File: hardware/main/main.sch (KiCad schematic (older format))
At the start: 62 parts, among them J1 Conn_01x10, J10 Conn_01x02, J11 Conn_01x02, J2 Conn_01x10, J3 Conn_01x02, J4 USB_B_Micro, J5 Conn_01x04, J6 Conn_01x03, J7 Conn_01x02, J8 Conn_01x03, J9 Conn_01x02, K1 G6SU-2, K2 G6SU-2, K3 G6SU-2, K4 G6SU-2, K5 G6SU-2, K6 G6SU-2, K7 G6SU-2, K8 G6SU-2, SW1 Rotary_Encoder_Switch, U1 NCV7726B, U10 SP3485EN, U2 MAX98357A, U3 MOC3043M, U4 SP3485EN, U5 E73-2G4M08S1C-52840, U6 BME680, U7 TPS82130, U8 D203S, U9 UG-2864ASWPG01

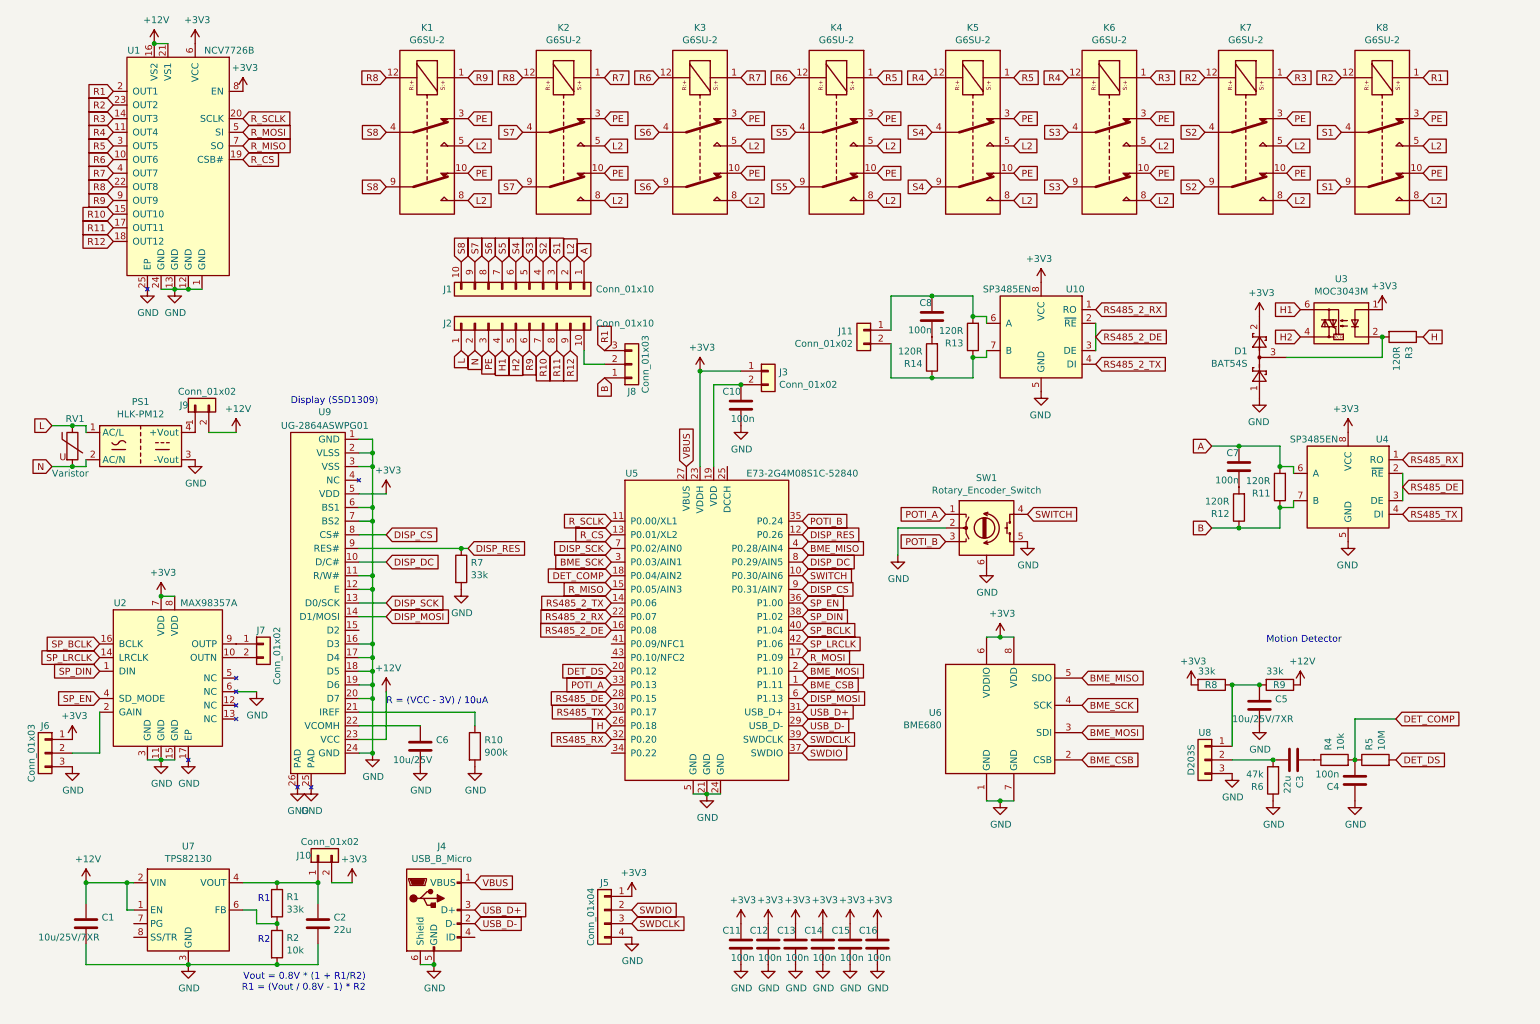
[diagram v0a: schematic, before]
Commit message: Update main board to use LIN
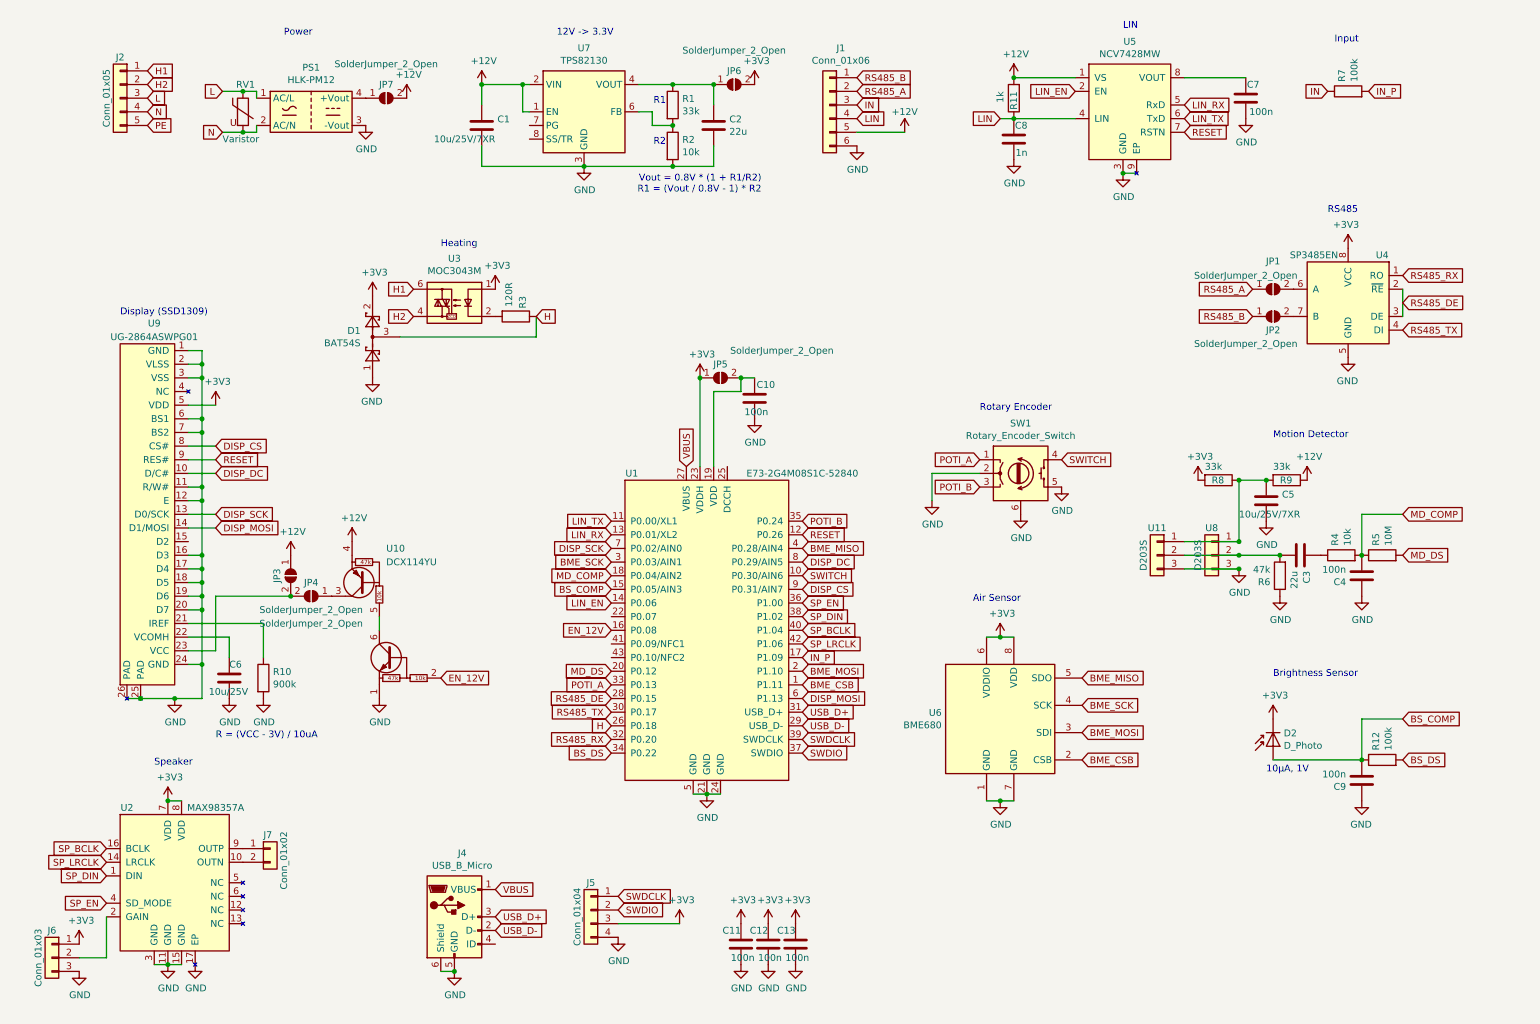
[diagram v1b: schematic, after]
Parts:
- removed C14, C15, C16: 100n, Capacitor_SMD:C_0603_1608Metric, symbol Device:C
- removed J1, J2: Conn_01x10, RoomControl:WAGO-236-410, symbol Connector_Generic:Conn_01x10
- removed J10, J3, J9: Conn_01x02, RoomControl:Jumper2, symbol Connector_Generic:Conn_01x02
- removed J11: Conn_01x02, Connector_PinHeader_2.54mm:PinHeader_1x02_P2.54mm_Vertical, symbol Connector_Generic:Conn_01x02
- removed J8: Conn_01x03, RoomControl:Jumper3, symbol Connector_Generic:Conn_01x03
- removed K1, K2, K3, K4, K5, K6, K7, K8: G6SU-2, RoomControl:Relay_DPDT_Omron_G6SU-2, symbol Relay:G6SU-2
- removed R13: 120R, Resistor_SMD:R_1206_3216Metric, symbol Device:R
- removed R14: 120R, Resistor_SMD:R_0603_1608Metric, symbol Device:R
- removed U1: NCV7726B, RoomControl:NCV7726B, symbol RoomControl:NCV7726B
- removed U10: SP3485EN, Package_SO:SOIC-8_3.9x4.9mm_P1.27mm, symbol Interface_UART:SP3485EN
- added C9: 100n, Capacitor_SMD:C_0603_1608Metric, symbol Device:C
- added D2: D_Photo, Connector_PinHeader_2.54mm:PinHeader_1x02_P2.54mm_Vertical, symbol Device:D_Photo
- added J1: Conn_01x06, RoomControl:Wago_236-406, symbol Connector_Generic:Conn_01x06
- added J2: Conn_01x05, RoomControl:Wago_236-405, symbol Connector_Generic:Conn_01x05
- added JP1, JP2, JP3, JP4, JP5, JP6, JP7: SolderJumper_2_Open, RoomControl:Jumper2Triangular, symbol Jumper:SolderJumper_2_Open
- added U10: DCX114YU, Package_TO_SOT_SMD:SOT-363_SC-70-6, symbol RoomControl:DCX114YU
- added U11: D203S, RoomControl:D203S, symbol Connector_Generic:Conn_01x03
- added U5: NCV7428MW, Package_DFN_QFN:DFN-8-1EP_3x3mm_P0.65mm_EP1.55x2.4mm, symbol RoomControl:NCV7428MW
- C8: value 100n -> 1n
- PS1: footprint Converter_ACDC:Converter_ACDC_HiLink_HLK-PMxx -> RoomControl:Converter_ACDC_HiLink_HLK-PMxx
- R11: value 120R -> 1k; footprint Resistor_SMD:R_1206_3216Metric -> Resistor_SMD:R_0603_1608Metric
- R12: value 120R -> 100k
- R7: value 33k -> 100k; footprint Resistor_SMD:R_0603_1608Metric -> Resistor_SMD:R_1206_3216Metric
- renumbered U5 to U1
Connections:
- net +12V: now also R11.2, J1.5 (Pin_5), JP3.1 (A), JP7.2 (B), U10.4 (C2), U5.1 (VS); no longer U9.23 (VCC)
- net +3V3: now also J5.3 (Pin_3), D2.1 (K), JP5.1 (A), JP6.2 (B); no longer J5.1 (Pin_1)
- net GND: now also C7.1, C8.1, C9.1, J1.6 (Pin_6), U10.1 (E1), U11.3 (Pin_3), U5.3 (GND), U5.9 (EP); no longer R7.2, U2.6 (NC)
- net H: now also D1.3
- net H1: now also J2.1 (Pin_1)
- net H2: now also J2.2 (Pin_2)
- net L: now also J2.3 (Pin_3)
- net N: now also J2.4 (Pin_4)
- net PE: now also J2.5 (Pin_5)
- net SWDCLK: now also J5.1 (Pin_1); no longer J5.3 (Pin_3)
- net at C2.1, R1.1, U7.4 (VOUT)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: now also JP6.1 (A)
- net at PS1.4 (+Vout): now also JP7.1 (A)
- net at R3.2, U3.2: no longer D1.3
- net at C10.2, U1.19 (VDD): now also JP5.2 (B)
- net BS_DS: now reaches U1.34 (P0.22)
- net BS_DS: now also R12.2
- net at C3.2, R6.2, U8.2 (Pin_2): now also U11.2 (Pin_2)
- net at C5.1, R8.1, R9.2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: now also U11.1 (Pin_1)
- net LIN: now reaches C8.2
- net LIN: now also R11.1, J1.4 (Pin_4), U5.4 (LIN)
- removed net A: C7.2, R11.2, U4.6 (A)
- removed net B: R11.1, R12.1, U4.7 (B)
- net DET_COMP renamed MD_COMP
- net DET_DS renamed MD_DS
- net DISP_RES renamed RESET
- net RESET: now also U5.7 (RSTN); no longer R7.1
- net RS485_2_DE renamed EN_12V
- net EN_12V: now also U10.2 (B1)
- net RS485_2_RX: no longer names the net of U1.22 (P0.07)
- net RS485_2_TX renamed LIN_EN
- net LIN_EN: now also U5.2 (EN)
- net R_CS renamed LIN_RX
- net LIN_RX: now also U5.5 (RxD)
- net R_MISO renamed BS_COMP
- net BS_COMP: now also R12.1, C9.2, D2.2 (A)
- net R_MOSI renamed IN_P
- net IN_P: now also R7.2
- net R_SCLK renamed LIN_TX
- net LIN_TX: now also U5.6 (TxD)
- new net: JP1.2 (B), U4.6 (A)
- new net: JP2.2 (B), U4.7 (B)
- new net: JP3.2 (B), JP4.2 (B), U9.23 (VCC)
- new net: C7.2, U5.8 (VOUT)
- new net: JP4.1 (A), U10.3 (C2)
- new net: U10.5 (B2), U10.6 (C1)
- new net IN: J1.3 (Pin_3), R7.1
- new net RS485_A: J1.2 (Pin_2), JP1.1 (A)
- new net RS485_B: J1.1 (Pin_1), JP2.1 (A)
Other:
- note added: "10µA, 1V"
- note added: "12V -> 3.3V"
- note added: "Air Sensor"
- note added: "Brightness Sensor"
- note added: "Heating"
- note added: "Input"
- note added: "LIN"
- note added: "Power"
- note added: "RS485"
- note added: "Rotary Encoder"
- note added: "Speaker"
- moved on the sheet: C1, C10, C2, C3, C4, C5, C6, D1, J4, J5, J6, J7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

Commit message: Add backup battery and 32768Hz crystal
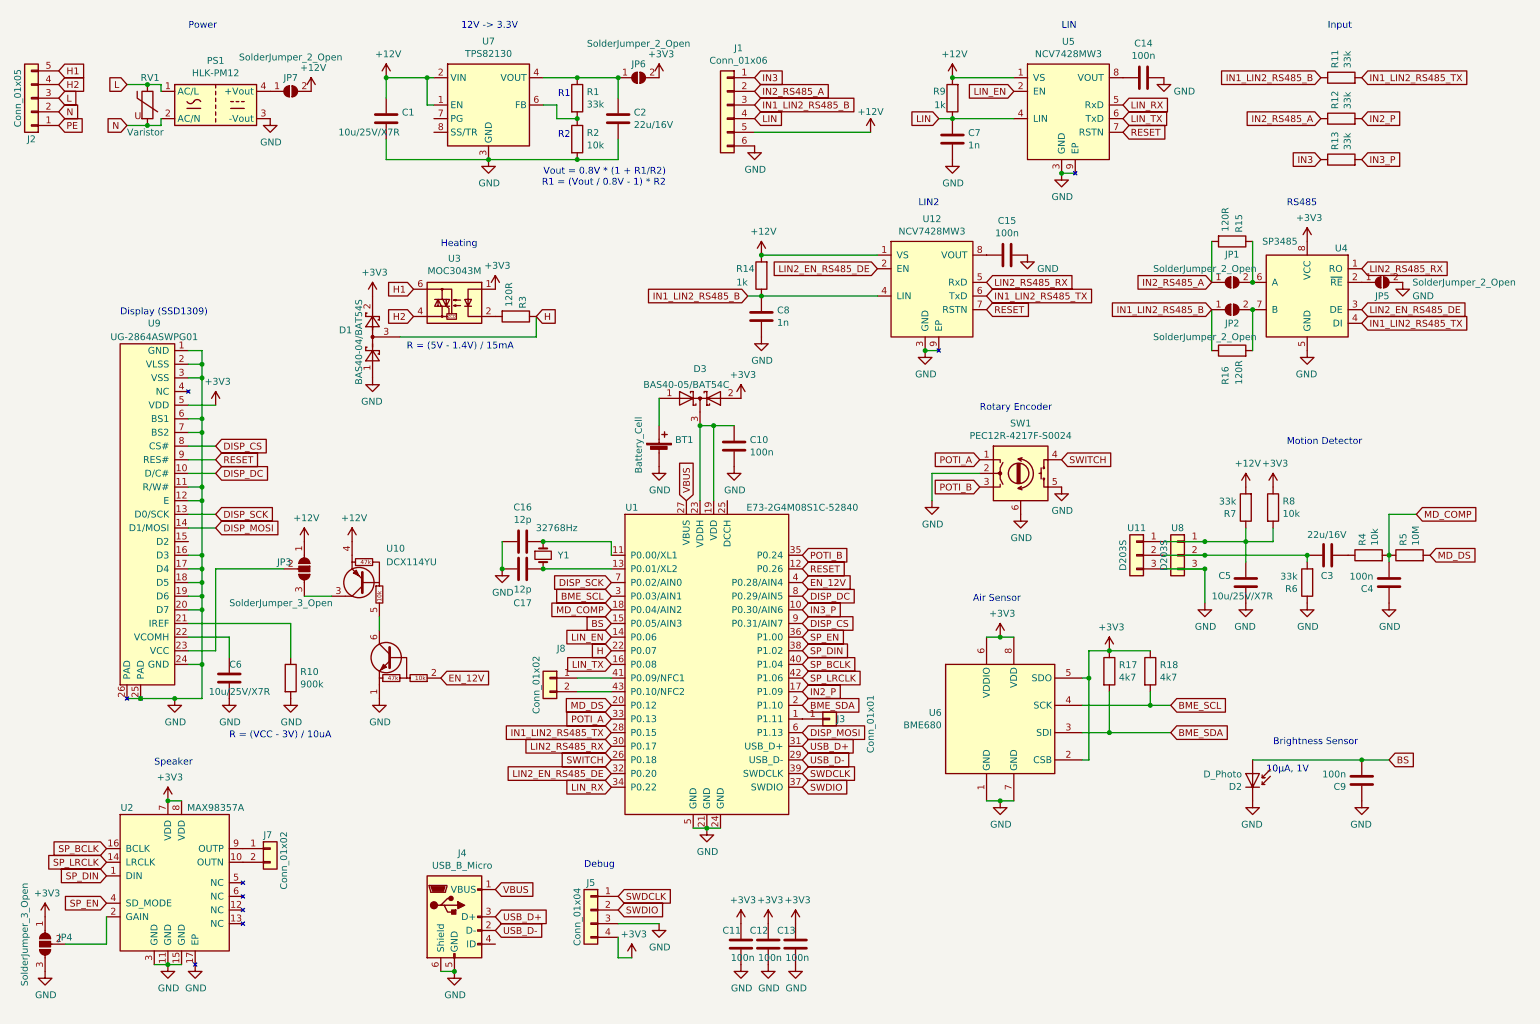
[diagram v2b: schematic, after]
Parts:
- removed J6: Conn_01x03, RoomControl:Jumper3, symbol Connector_Generic:Conn_01x03
- removed JP3, JP4: SolderJumper_2_Open, RoomControl:Jumper2Triangular, symbol Jumper:SolderJumper_2_Open
- removed R11: 1k, Resistor_SMD:R_0603_1608Metric, symbol Device:R
- added BT1: Battery_Cell, RoomControl:Battery_2032, symbol Device:Battery_Cell
- added C14, C15: 100n, Capacitor_SMD:C_0603_1608Metric, symbol Device:C
- added C16, C17: 12p, Capacitor_SMD:C_0603_1608Metric, symbol Device:C
- added D3: BAS40-05/BAT54C, Package_TO_SOT_SMD:SOT-23, symbol Device:D_Schottky_x2_KCom_AAK
- added J3: Conn_01x01, RoomControl:Pad, symbol Connector_Generic:Conn_01x01
- added J8: Conn_01x02, Connector_PinHeader_2.00mm:PinHeader_1x02_P2.00mm_Vertical, symbol Connector_Generic:Conn_01x02
- added JP3, JP4: SolderJumper_3_Open, RoomControl:Jumper3, symbol Jumper:SolderJumper_3_Open
- added R13: 33k, Resistor_SMD:R_1206_3216Metric, symbol Device:R
- added R14: 1k, Resistor_SMD:R_1206_3216Metric, symbol Device:R
- added R15, R16: 120R, Resistor_SMD:R_1206_3216Metric, symbol Device:R
- added R17, R18: 4k7, Resistor_SMD:R_0603_1608Metric, symbol Device:R
- added R7: 33k, Resistor_SMD:R_0603_1608Metric, symbol Device:R
- added U12: NCV7428MW3, RoomControl:On_NCV7428MW, symbol RoomControl:NCV7428MW
- added Y1: 32768Hz, Crystal:Crystal_DS26_D2.0mm_L6.0mm_Vertical, symbol Device:Crystal_Small
- C1, C5: value 10u/25V/7XR -> 10u/25V/X7R
- C2, C3: value 22u -> 22u/16V
- C6: value 10u/25V -> 10u/25V/X7R
- C7: value 100n -> 1n
- D1: value BAT54S -> BAS40-04/BAT54S
- JP1, JP2, JP5, JP6, JP7: footprint RoomControl:Jumper2Triangular -> RoomControl:Jumper2
- PS1: footprint RoomControl:Converter_ACDC_HiLink_HLK-PMxx -> RoomControl:HiLink_HLK-PMxx
- R11: renamed from R7; value 100k -> 33k
- R12: value 100k -> 33k; footprint Resistor_SMD:R_0603_1608Metric -> Resistor_SMD:R_1206_3216Metric
- R6: value 47k -> 33k
- R8: value 33k -> 10k
- R9: value 33k -> 1k; footprint Resistor_SMD:R_0603_1608Metric -> Resistor_SMD:R_1206_3216Metric
- SW1: value Rotary_Encoder_Switch -> PEC12R-4217F-S0024; footprint RoomControl:ALPS-BOURNS-EC12 -> RoomControl:Bourns_PEC12R
- U3: footprint RoomControl:MOC3043 -> RoomControl:On_MOC3043
- U4: value SP3485EN -> SP3485
- U5: value NCV7428MW -> NCV7428MW3; footprint Package_DFN_QFN:DFN-8-1EP_3x3mm_P0.65mm_EP1.55x2.4mm -> RoomControl:On_NCV7428MW
- U6: footprint Package_LGA:Bosch_LGA-8_3x3mm_P0.8mm_ClockwisePinNumbering -> RoomControl:Bosch_BME680
- U7: footprint RoomControl:TPS82130 -> RoomControl:Texas_TPS82130
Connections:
- net +12V: now also R9.2, JP3.1 (A), R14.2, R7.2, U12.1 (VS); no longer R9.1
- net +3V3: now also J5.4 (Pin_4), R8.1, U6.2 (CSB), U6.5 (SDO), D3.2 (A), JP4.1 (A), R17.1, R18.1; no longer D2.1 (K), J5.3 (Pin_3), JP5.1 (A), R8.2, U1.23 (VDDH)
- net EN_12V: now also U1.4 (P0.28/AIN4); no longer U1.16 (P0.08)
- net GND: now also C10.2, C7.2, C8.2, D2.1 (K), J5.3 (Pin_3), JP5.2 (B), BT1.2 (-), C14.1, C15.1, C16.2, C17.2, JP4.3 (B), U12.3 (GND), U12.9 (EP); no longer C10.1, C7.1, C8.1, J5.4 (Pin_4)
- net H: now also U1.22 (P0.07); no longer U1.26 (P0.18)
- net H1: now also J2.5 (Pin_5); no longer J2.1 (Pin_1)
- net H2: now also J2.4 (Pin_4); no longer J2.2 (Pin_2)
- net LIN: now also C7.1, R9.1; no longer C8.2
- net LIN_RX: now also U1.34 (P0.22); no longer U1.13 (P0.01/XL2)
- net LIN_TX: now also U1.16 (P0.08); no longer U1.11 (P0.00/XL1)
- net N: now also J2.2 (Pin_2); no longer J2.4 (Pin_4)
- net PE: now also J2.1 (Pin_1); no longer J2.5 (Pin_5)
- net RESET: now also U12.7 (RSTN)
- net SWITCH: now also U1.26 (P0.18); no longer U1.10 (P0.30/AIN6)
- net at U1.41 (P0.09/NFC1): now also J8.1 (Pin_1)
- net at U1.43 (P0.10/NFC2): now also J8.2 (Pin_2)
- net at JP1.2 (B), U4.6 (A): now also R15.1
- net at JP2.2 (B), U4.7 (B): now also R16.2
- net at U2.2 (GAIN): now also JP4.2 (C)
- net at U9.23 (VCC): now also JP3.2 (C)
- net at C5.1, U11.1 (Pin_1), U8.1 (Pin_1): now also R8.2, R7.1; no longer R8.1, R9.2
- net at U5.8 (VOUT): now also C14.2; no longer C7.2
- net at U10.3 (C2): now also JP3.3 (B)
- net BME_CSB: no longer names the net of U1.1 (P1.11)
- net BME_CSB: now also J3.1 (Pin_1); no longer U6.2 (CSB)
- removed net BME_MISO: U1.4 (P0.28/AIN4), U6.5 (SDO)
- net BME_MOSI renamed BME_SDA
- net BME_SDA: now also R17.2
- net BME_SCK renamed BME_SCL
- net BME_SCL: now also R18.2
- net BS_COMP renamed BS
- net BS: no longer R12.1
- net BS_DS renamed IN2_P
- net IN2_P: now also U1.17 (P1.09); no longer U1.34 (P0.22)
- net IN renamed IN1_LIN2_RS485_B
- net IN1_LIN2_RS485_B: now also C8.1, JP2.1 (A), R14.1, R16.1, U12.4 (LIN)
- net IN_P renamed IN1_LIN2_RS485_TX
- net IN1_LIN2_RS485_TX: now also U1.28 (P0.15), U4.4 (DI), U12.6 (TxD); no longer U1.17 (P1.09)
- net RS485_A renamed IN2_RS485_A
- net IN2_RS485_A: now also R12.1, R15.2
- net RS485_B renamed IN3
- net IN3: now also R13.1; no longer JP2.1 (A)
- removed net RS485_DE: U1.28 (P0.15), U4.2 (~RE~), U4.3 (DE)
- net RS485_RX renamed LIN2_EN_RS485_DE
- net LIN2_EN_RS485_DE: now also U4.3 (DE), U12.2 (EN); no longer U4.1 (RO)
- net RS485_TX renamed LIN2_RS485_RX
- net LIN2_RS485_RX: now also U4.1 (RO), U12.5 (RxD); no longer U4.4 (DI)
- new net: C16.1, U1.11 (P0.00/XL1), Y1.1
- new net: C17.1, U1.13 (P0.01/XL2), Y1.2
- new net: C10.1, D3.3 (K), U1.19 (VDD), U1.23 (VDDH)
- new net: JP5.1 (A), U4.2 (~RE~)
- new net: BT1.1 (+), D3.1 (A)
- new net: C15.2, U12.8 (VOUT)
- new net IN3_P: R13.2, U1.10 (P0.30/AIN6)
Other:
- note added: "Debug"
- note added: "LIN2"
- note added: "R = (5V - 1.4V) / 15mA"
- moved on the sheet: C1, C2, C3, C4, C5, D2, J1, J2, JP1, JP2, JP6, JP7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

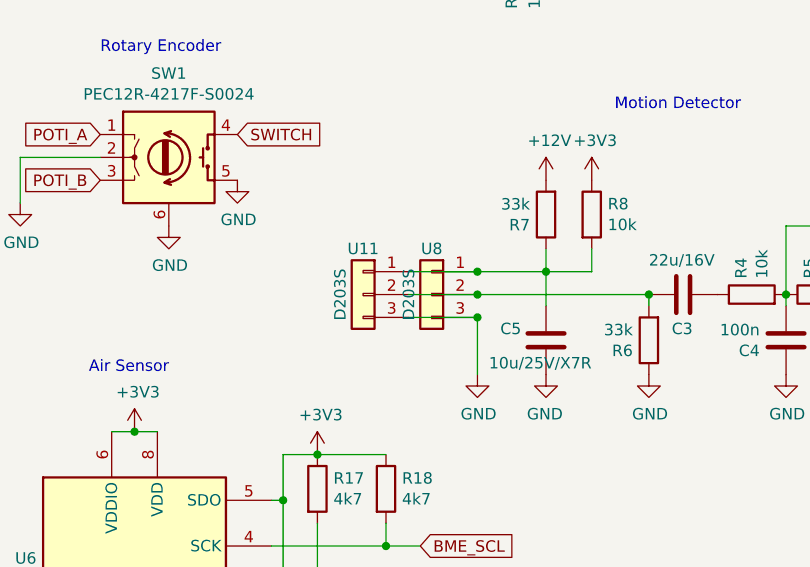
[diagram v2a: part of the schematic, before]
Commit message: New speaker and pir sensor lens
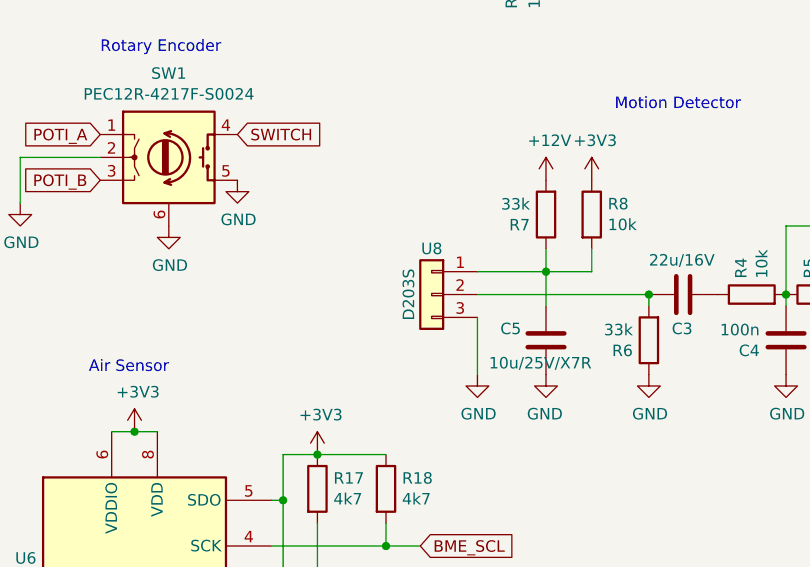
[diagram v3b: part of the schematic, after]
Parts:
- removed U11: D203S, RoomControl:D203S, symbol Connector_Generic:Conn_01x03
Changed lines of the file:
@@
 10µA, 1V
-$Comp
-L Connector_Generic:Conn_01x03 U11
-U 1 1 5EF5F588
-P 8750 4500
-F 0 "U11" H 8750 4700 50  0000 C CNN
-F 1 "D203S" V 8850 4500 50  0000 C CNN
-F 2 "RoomControl:D203S" H 8750 4500 50  0001 C CNN
-F 3 "~" H 8750 4500 50  0001 C CNN
-	1    8750 4500
-	-1   0    0    -1
-$EndComp
-Wire Wire Line
-	8950 4400 9250 4400
-Wire Wire Line
-	8950 4500 9250 4500
-Connection ~ 9250 4500
-Wire Wire Line
-	8950 4600 9250 4600
-Connection ~ 9250 4600
 $Comp
 L Device:Battery_Cell BT1
@@
 Wire Wire Line
 	9250 4400 9550 4400
-Connection ~ 9250 4400
 Connection ~ 9550 4400
 Text Notes 3400 3000 0    50   ~ 0
